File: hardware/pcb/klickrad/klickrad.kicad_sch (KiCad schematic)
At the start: 22 parts, among them J1 FH12-6S-0.5SH, SW1 BUTTON, SW2 WHEEL, SW3 GUARD, U1 AT42QT2120, U2 DRV2605LDGSR

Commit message: Hauptplatine: platziert, nicht geroutet; Befund in KONZEPT.md
Co-Authored-By: Claude Sonnet 5.5 <noreply@anthropic.com>
Claude-Session: https://claude.ai/code/session_01JifvE6gExGmwsJWDpfRrrS
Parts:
- removed C5: 10uF, Capacitor_SMD:C_0603_1608Metric, symbol Device:C
- J1: value FH12-6S-0.5SH -> 503480-0600; footprint Connector_FFC-FPC:Hirose_FH12-6S-0.5SH_1x06-1MP_P0.50mm_Horizontal -> Klickrad:Molex_503480-0600_1x06-1MP_P0.50mm_Horizontal; Beschreibung FFC/FPC 6-pol., 0,5 mm, Flip-Lock, Bauhöhe 1,0 mm; Pin 6 = 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 -> FFC/FPC 6-pol., 0,5 mm, Easy-On, Dual Contact, Bauhöhe 1,0 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; Hersteller Hirose -> Molex; MPN FH12-6S-0.5SH(55) -> 503480-0600
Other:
- note added: "DRV2605L: VDD 1 uF, REG 1 uF, EN-Pull-up (wie Tangara)"
- note removed: "DRV2605L: VDD 1 uF (+ 10 uF fuer den LRA-Strom), REG 1 uF, EN-Pull-up"
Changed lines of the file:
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@@
 	(symbol (lib_id "Connector_Generic:Conn_01x06") (at 39.37 105.41 0) (unit 1) (exclude_from_sim no) (in_bom yes) (on_board yes) (dnp no)
 		(property "Reference" "J1" (at 39.37 93.41 0) (effects (font (size 1.27 1.27)) (justify left)))
-		(property "Value" "FH12-6S-0.5SH" (at 39.37 117.41 0) (effects (font (size 1.27 1.27)) (justify left)))
-		(property "Footprint" "Connector_FFC-FPC:Hirose_FH12-6S-0.5SH_1x06-1MP_P0.50mm_Horizontal" (at 42.37 105.41 0) (effects (font (size 1.27 1.27)) (justify left) (hide yes)))
+		(property "Value" "503480-0600" (at 39.37 117.41 0) (effects (font (size 1.27 1.27)) (justify left)))
+		(property "Footprint" "Klickrad:Molex_503480-0600_1x06-1MP_P0.50mm_Horizontal" (at 42.37 105.41 0) (effects (font (size 1.27 1.27)) (justify left) (hide yes)))
 		(property "Datasheet" "" (at 42.37 105.41 0) (effects (font (size 1.27 1.27)) (justify left) (hide yes)))
-		(property "MPN" "FH12-6S-0.5SH(55)" (at 42.37 105.41 0) (effects (font (size 1.27 1.27)) (justify left) (hide yes)))
-		(property "Hersteller" "Hirose" (at 42.37 105.41 0) (effects (font (size 1.27 1.27)) (justify left) (hide yes)))
-		(property "Beschreibung" "FFC/FPC 6-pol., 0,5 mm, Flip-Lock, Bauhöhe 1,0 mm; Pin 6 = Reserve (BTN)" (at 42.37 105.41 0) (effects (font (size 1.27 1.27)) (justify left) (hide yes)))
+		(property "MPN" "503480-0600" (at 42.37 105.41 0) (effects (font (size 1.27 1.27)) (justify left) (hide yes)))
+		(property "Hersteller" "Molex" (at 42.37 105.41 0) (effects (font (size 1.27 1.27)) (justify left) (hide yes)))
+		(property "Beschreibung" "FFC/FPC 6-pol., 0,5 mm, Easy-On, Dual Contact, Bauhöhe 1,0 mm; Pin 6 = Reserve (BTN)" (at 42.37 105.41 0) (effects (font (size 1.27 1.27)) (justify left) (hide yes)))
 		(pin "1")
 		(pin "2")
@@
 		(instances (project "klickrad" (path "/d0653523-91ed-5abf-874a-42a7dd1abc8f" (reference "#PWR15") (unit 1))))
 	)
-	(symbol (lib_id "Device:C") (at 220.98 160.02 0) (unit 1) (exclude_from_sim no) (in_bom yes) (on_board yes) (dnp no)
-		(property "Reference" "C5" (at 223.98 157.48 0) (effects (font (size 1.27 1.27)) (justify left)))
-		(property "Value" "10uF" (at 223.98 162.56 0) (effects (font (size 1.27 1.27)) (justify left)))
-		(property "Footprint" "Capacitor_SMD:C_0603_1608Metric" (at 223.98 160.02 0) (effects (font (size 1.27 1.27)) (justify left) (hide yes)))
+	(symbol (lib_id "Device:R") (at 220.98 160.02 0) (unit 1) (exclude_from_sim no) (in_bom yes) (on_board yes) (dnp no)
+		(property "Reference" "R7" (at 223.98 157.48 0) (effects (font (size 1.27 1.27)) (justify left)))
+		(property "Value" "10k" (at 223.98 162.56 0) (effects (font (size 1.27 1.27)) (justify left)))
+		(property "Footprint" "Resistor_SMD:R_0402_1005Metric" (at 223.98 160.02 0) (effects (font (size 1.27 1.27)) (justify left) (hide yes)))
 		(property "Datasheet" "" (at 223.98 160.02 0) (effects (font (size 1.27 1.27)) (justify left) (hide yes)))
-		(property "Beschreibung" "LRA-Stromspitzen (neu gegenueber Tangara)" (at 223.98 160.02 0) (effects (font (size 1.27 1.27)) (justify left) (hide yes)))
-		(pin "1")
-		(pin "2")
-		(instances (project "klickrad" (path "/d0653523-91ed-5abf-874a-42a7dd1abc8f" (reference "C5") (unit 1))))
+		(property "Beschreibung" "DRV2605L EN-Pull-up (Tangara R4)" (at 223.98 160.02 0) (effects (font (size 1.27 1.27)) (justify left) (hide yes)))
+		(pin "1")
+		(pin "2")
+		(instances (project "klickrad" (path "/d0653523-91ed-5abf-874a-42a7dd1abc8f" (reference "R7") (unit 1))))
 	)
 	(wire (pts (xy 220.98 156.21) (xy 220.98 153.67)) (stroke (width 0) (type default)))
@@
 	)
 	(wire (pts (xy 220.98 163.83) (xy 220.98 166.37)) (stroke (width 0) (type default)))
-	(symbol (lib_id "power:GND") (at 220.98 166.37 0) (unit 1) (exclude_from_sim no) (in_bom no) (on_board yes) (dnp no)
-		(property "Reference" "#PWR17" (at 223.98 163.83 0) (effects (font (size 1.27 1.27)) (justify left) (hide yes)))
-		(property "Value" "GND" (at 223.98 168.91 0) (effects (font (size 1.27 1.27)) (justify left)))
-		(property "Footprint" "" (at 223.98 166.37 0) (effects (font (size 1.27 1.27)) (justify left) (hide yes)))
-		(property "Datasheet" "" (at 223.98 166.37 0) (effects (font (size 1.27 1.27)) (justify left) (hide yes)))
-		(pin "1")
-		(instances (project "klickrad" (path "/d0653523-91ed-5abf-874a-42a7dd1abc8f" (reference "#PWR17") (unit 1))))
-	)
-	(symbol (lib_id "Device:R") (at 236.22 160.02 0) (unit 1) (exclude_from_sim no) (in_bom yes) (on_board yes) (dnp no)
-		(property "Reference" "R7" (at 239.22 157.48 0) (effects (font (size 1.27 1.27)) (justify left)))
-		(property "Value" "10k" (at 239.22 162.56 0) (effects (font (size 1.27 1.27)) (justify left)))
-		(property "Footprint" "Resistor_SMD:R_0402_1005Metric" (at 239.22 160.02 0) (effects (font (size 1.27 1.27)) (justify left) (hide yes)))
-		(property "Datasheet" "" (at 239.22 160.02 0) (effects (font (size 1.27 1.27)) (justify left) (hide yes)))
-		(property "Beschreibung" "DRV2605L EN-Pull-up (Tangara R4)" (at 239.22 160.02 0) (effects (font (size 1.27 1.27)) (justify left) (hide yes)))
-		(pin "1")
-		(pin "2")
-		(instances (project "klickrad" (path "/d0653523-91ed-5abf-874a-42a7dd1abc8f" (reference "R7") (unit 1))))
-	)
-	(wire (pts (xy 236.22 156.21) (xy 236.22 153.67)) (stroke (width 0) (type default)))
-	(symbol (lib_id "power:+3V3") (at 236.22 153.67 0) (unit 1) (exclude_from_sim no) (in_bom no) (on_board yes) (dnp no)
-		(property "Reference" "#PWR18" (at 239.22 151.13 0) (effects (font (size 1.27 1.27)) (justify left) (hide yes)))
-		(property "Value" "3V3" (at 239.22 156.21 0) (effects (font (size 1.27 1.27)) (justify left)))
-		(property "Footprint" "" (at 239.22 153.67 0) (effects (font (size 1.27 1.27)) (justify left) (hide yes)))
-		(property "Datasheet" "" (at 239.22 153.67 0) (effects (font (size 1.27 1.27)) (justify left) (hide yes)))
-		(pin "1")
-		(instances (project "klickrad" (path "/d0653523-91ed-5abf-874a-42a7dd1abc8f" (reference "#PWR18") (unit 1))))
-	)
-	(wire (pts (xy 236.22 163.83) (xy 236.22 166.37)) (stroke (width 0) (type default)))
-	(global_label "EN" (shape passive) (at 236.22 166.37 270) (fields_autoplaced yes) (effects (font (size 1.27 1.27)) (justify right))
-		(property "Intersheetrefs" "${INTERSHEET_REFS}" (at 236.22 166.37 0) (effects (font (size 1.27 1.27)) (hide yes)))
-	)
-	(text "DRV2605L: VDD 1 uF (+ 10 uF fuer den LRA-Strom), REG 1 uF, EN-Pull-up" (exclude_from_sim no) (at 188 150 0) (effects (font (size 1.27 1.27) bold) (justify left bottom)))
+	(global_label "EN" (shape passive) (at 220.98 166.37 270) (fields_autoplaced yes) (effects (font (size 1.27 1.27)) (justify right))
+		(property "Intersheetrefs" "${INTERSHEET_REFS}" (at 220.98 166.37 0) (effects (font (size 1.27 1.27)) (hide yes)))
+	)
+	(text "DRV2605L: VDD 1 uF, REG 1 uF, EN-Pull-up (wie Tangara)" (exclude_from_sim no) (at 188 150 0) (effects (font (size 1.27 1.27) bold) (justify left bottom)))
 	(symbol (lib_id "Connector:TestPoint") (at 265.43 105.41 0) (unit 1) (exclude_from_sim no) (in_bom no) (on_board yes) (dnp no)
 		(property "Reference" "TP1" (at 268.43 102.87 0) (effects (font (size 1.27 1.27)) (justify left)))
@@
 	(wire (pts (xy 115.57 241.3) (xy 115.57 238.76)) (stroke (width 0) (type default)))
 	(symbol (lib_id "power:+3V3") (at 115.57 238.76 0) (unit 1) (exclude_from_sim no) (in_bom no) (on_board yes) (dnp no)
-		(property "Reference" "#PWR19" (at 118.57 236.22 0) (effects (font (size 1.27 1.27)) (justify left) (hide yes)))
+		(property "Reference" "#PWR17" (at 118.57 236.22 0) (effects (font (size 1.27 1.27)) (justify left) (hide yes)))
 		(property "Value" "3V3" (at 118.57 241.3 0) (effects (font (size 1.27 1.27)) (justify left)))
 		(property "Footprint" "" (at 118.57 238.76 0) (effects (font (size 1.27 1.27)) (justify left) (hide yes)))
 		(property "Datasheet" "" (at 118.57 238.76 0) (effects (font (size 1.27 1.27)) (justify left) (hide yes)))
 		(pin "1")
-		(instances (project "klickrad" (path "/d0653523-91ed-5abf-874a-42a7dd1abc8f" (reference "#PWR19") (unit 1))))
+		(instances (project "klickrad" (path "/d0653523-91ed-5abf-874a-42a7dd1abc8f" (reference "#PWR17") (unit 1))))
 	)
 	(wire (pts (xy 115.57 248.92) (xy 115.57 251.46)) (stroke (width 0) (type default)))
@@
 	(wire (pts (xy 130.81 241.3) (xy 130.81 238.76)) (stroke (width 0) (type default)))
 	(symbol (lib_id "power:+3V3") (at 130.81 238.76 0) (unit 1) (exclude_from_sim no) (in_bom no) (on_board yes) (dnp no)
-		(property "Reference" "#PWR20" (at 133.81 236.22 0) (effects (font (size 1.27 1.27)) (justify left) (hide yes)))
+		(property "Reference" "#PWR18" (at 133.81 236.22 0) (effects (font (size 1.27 1.27)) (justify left) (hide yes)))
 		(property "Value" "3V3" (at 133.81 241.3 0) (effects (font (size 1.27 1.27)) (justify left)))
 		(property "Footprint" "" (at 133.81 238.76 0) (effects (font (size 1.27 1.27)) (justify left) (hide yes)))
 		(property "Datasheet" "" (at 133.81 238.76 0) (effects (font (size 1.27 1.27)) (justify left) (hide yes)))
 		(pin "1")
-		(instances (project "klickrad" (path "/d0653523-91ed-5abf-874a-42a7dd1abc8f" (reference "#PWR20") (unit 1))))
+		(instances (project "klickrad" (path "/d0653523-91ed-5abf-874a-42a7dd1abc8f" (reference "#PWR18") (unit 1))))
 	)
 	(wire (pts (xy 130.81 248.92) (xy 130.81 251.46)) (stroke (width 0) (type default)))

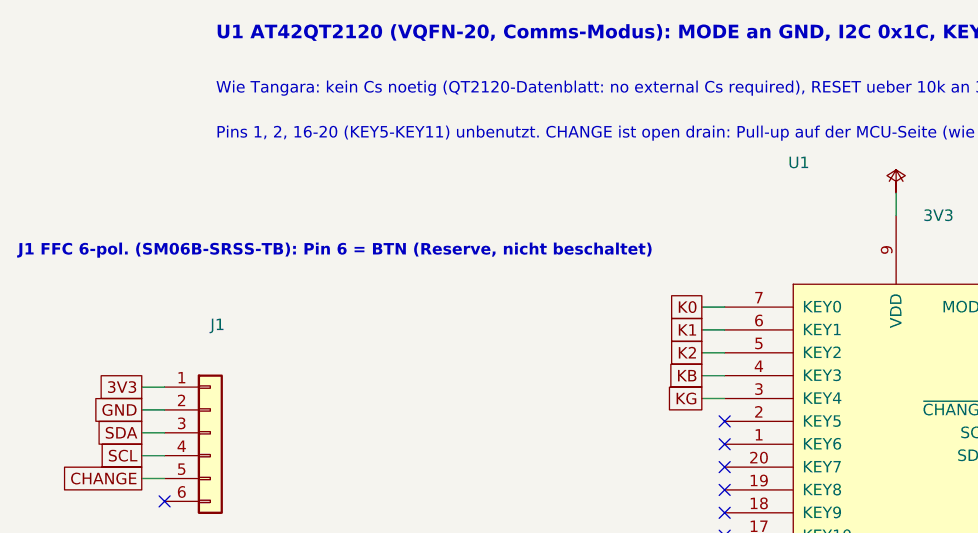
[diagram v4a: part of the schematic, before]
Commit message: Klickrad J1 auf J21-Landmuster, neu geroutet; TEILE-Nachtrag
Co-Authored-By: Claude Sonnet 5.5 <noreply@anthropic.com>
Claude-Session: https://claude.ai/code/session_01JifvE6gExGmwsJWDpfRrrS
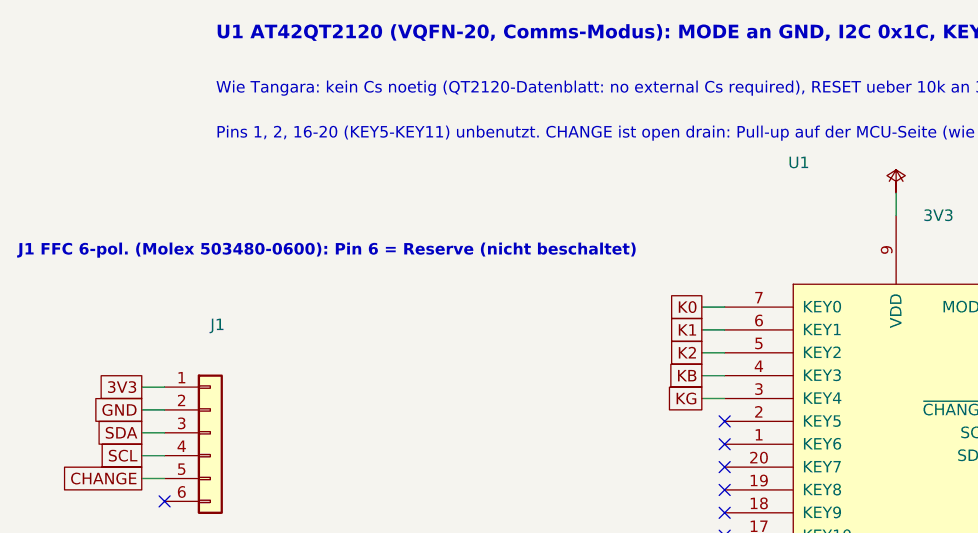
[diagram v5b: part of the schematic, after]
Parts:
- J1: footprint Klickrad:Molex_503480-0600_1x06-1MP_P0.50mm_Horizontal -> Klickrad:Molex_503480-0600_Hauptplatine
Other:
- note added: "J1 FFC 6-pol. (Molex 503480-0600): Pin 6 = Reserve (nicht beschaltet)"
- note removed: "J1 FFC 6-pol. (SM06B-SRSS-TB): Pin 6 = BTN (Reserve, nicht beschaltet)"
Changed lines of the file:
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@@
 		(property "Reference" "J1" (at 39.37 93.41 0) (effects (font (size 1.27 1.27)) (justify left)))
 		(property "Value" "503480-0600" (at 39.37 117.41 0) (effects (font (size 1.27 1.27)) (justify left)))
-		(property "Footprint" "Klickrad:Molex_503480-0600_1x06-1MP_P0.50mm_Horizontal" (at 42.37 105.41 0) (effects (font (size 1.27 1.27)) (justify left) (hide yes)))
+		(property "Footprint" "Klickrad:Molex_503480-0600_Hauptplatine" (at 42.37 105.41 0) (effects (font (size 1.27 1.27)) (justify left) (hide yes)))
 		(property "Datasheet" "" (at 42.37 105.41 0) (effects (font (size 1.27 1.27)) (justify left) (hide yes)))
 		(property "MPN" "503480-0600" (at 42.37 105.41 0) (effects (font (size 1.27 1.27)) (justify left) (hide yes)))
@@
 	)
 	(no_connect (at 34.29 113.03))
-	(text "J1 FFC 6-pol. (SM06B-SRSS-TB): Pin 6 = BTN (Reserve, nicht beschaltet)" (exclude_from_sim no) (at 18 86 0) (effects (font (size 1.27 1.27) bold) (justify left bottom)))
+	(text "J1 FFC 6-pol. (Molex 503480-0600): Pin 6 = Reserve (nicht beschaltet)" (exclude_from_sim no) (at 18 86 0) (effects (font (size 1.27 1.27) bold) (justify left bottom)))
 	(symbol (lib_id "Driver_Haptic:DRV2605LDGS") (at 214.63 105.41 0) (unit 1) (exclude_from_sim no) (in_bom yes) (on_board yes) (dnp no)
 		(property "Reference" "U2" (at 202.63 87.41 0) (effects (font (size 1.27 1.27)) (justify left)))
